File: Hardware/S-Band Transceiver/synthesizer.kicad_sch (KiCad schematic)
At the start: 1 part, among them U10 ADF4351

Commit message: Working on schematic for adf4351
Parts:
- added C10, C11, C12, C20, C23, C25, C27, C29, C31: 10pF, symbol Device:C_Small
- added C13, C14, C15, C21, C22, C24, C26, C28, C30: 100nF, symbol Device:C_Small
- added C16: 39nF, symbol Device:C_Small
- added C17: 2.7nF, symbol Device:C_Small
- added C18: 1.2nF, symbol Device:C_Small
- added C19: 10nF, symbol Device:C_Small
- added J3: SMA, symbol Connector:Conn_Coaxial
- added R5: 4.7k, symbol Device:R_Small_US
- added R6: 680, symbol Device:R_Small_US
- added R7: 360, symbol Device:R_Small_US
- added R8, R9: 0, symbol Device:R_Small_US
- added X1: XO32, Oscillator:Oscillator_SMD_EuroQuartz_XO91-4Pin_7.0x5.0mm, symbol Oscillator:XO32
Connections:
- net SCLK: now reaches U10.1 (CLK)
- net +3V3: now reaches U10.10 (AVDD)
- net +3V3: now also U10.16 (VVCO), U10.17 (VVCO), U10.28 (DVDD), U10.32 (SDVDD), U10.4 (CE), U10.6 (Vp), C20.1, C21.1, C22.1, C23.1, C24.1, C25.1, C26.2, C27.2, C28.2, C29.2, C30.2, C31.2, X1.4 (V+)
- net GND: now reaches U10.11 (AGNDVCO)
- net GND: now also U10.18 (AGNDVCO), U10.21 (AGNDVCO), U10.27 (DGND), U10.31 (SDGND), U10.33 (EP), U10.8 (CPGND), U10.9 (AGND), C10.1, C11.1, C12.1, C13.1, C14.1, C15.1, C20.2, C21.2, C22.2, C23.2, C24.2, C25.2, C26.1, C27.1, C28.1, C29.1, C30.1, C31.1, J3.2 (Ext), R5.2, X1.2 (GND)
- net at U10.19 (TEMP): now also C12.2, C14.2
- net MOSI: now reaches U10.2 (DATA)
- net at U10.20 (VTUNE): now also C18.2, R6.2
- net at U10.22 (RSET): now also R5.1
- net at U10.23 (VCOM): now also C11.2, C13.2
- net at U10.24 (VREF): now also C10.2, C15.2
- net LD: now reaches U10.25 (LD)
- net PDB_RF: now reaches U10.26 (PDB_RF)
- net at U10.29 (REFIN): now also C19.1
- net ~{CS}: now reaches U10.3 (LE)
- net MUXOUT: now reaches U10.30 (MUXOUT)
- net at U10.7 (CPout): now also C16.2, C17.2, R6.1
- new net: C17.1, C18.1, R7.1
- new net: C16.1, R7.2
- new net EXT_REF: J3.1 (In), R9.1
- new net REF_IN: C19.2, R8.2, R9.2
- new net XO_EN: X1.1 (EN)
- new net XO_REF: R8.1, X1.3 (OUT)
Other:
- moved on the sheet: U10

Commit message: Updating schematic
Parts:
- added C44, C50: 100nF, symbol Device:C_Small
- added C45, C46, C49, C51: 120pF, symbol Device:C_Small
- added C47, C48, C52, C53: 1nF, symbol Device:C_Small
- added J5: SMA, symbol Connector:Conn_Coaxial
- added L10, L13, L14, L9: 1.9nH, symbol Device:L_Small
- added L11, L12, L7, L8: 7.5nH, symbol Device:L_Small
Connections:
- net GND: now also C44.2, C45.2, C46.2, C49.2, C50.2, C51.2, J5.2 (Ext)
- net at U10.12 (RF_OUT_A+): now also C52.1, L11.1
- net at U10.13 (RF_OUT_A-): now also C53.1, L12.2
- net at U10.14 (RF_OUT_B+): now also C48.1, L8.1
- net at U10.15 (RF_OUT_B-): now also C47.1, L7.2
- new net: C48.2, L10.1
- new net: C49.1, C50.1, C51.1, L11.2, L12.1
- new net: J5.1 (In), L14.2
- new net: C52.2, L13.1
- new net: C47.2, L9.1
- new net: C53.2, L14.1
- new net: C44.1, C45.1, C46.1, L7.1, L8.2
- new net LO+: L10.2
- new net LO-: L9.2

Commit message: Updating schematic
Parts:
- added C54: 100nF, symbol Device:C_Small
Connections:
- net +3V3: now also C54.1; no longer C24.1, C25.1, C26.2, C27.2, U10.16 (VVCO), U10.17 (VVCO), U10.4 (CE)
- net GND: now also C54.2
- new net +3V3PLL: C24.1, C25.1, C26.2, C27.2, U10.16 (VVCO), U10.17 (VVCO), U10.4 (CE)
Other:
- moved on the sheet: J3, R8, R9, X1

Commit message: Updating schematic
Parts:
- X1: footprint Oscillator:Oscillator_SMD_EuroQuartz_XO91-4Pin_7.0x5.0mm -> Oscillator:Oscillator_SMD_EuroQuartz_XO32-4Pin_3.2x2.5mm
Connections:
- net +3V3PLL: now also C44.1, C45.1, C46.1, C49.1, C50.1, C51.1, L11.2, L12.1, L7.1, L8.2
- net SYNTH_TX: now reaches L13.2
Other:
- note added: "0dBm"
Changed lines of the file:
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@@
 	(wire
 		(pts
+			(xy 214.63 72.39) (xy 215.9 72.39)
+		)
+		(stroke
+			(width 0)
+			(type default)
+		)
+	)
+	(wire
+		(pts
 			(xy 88.9 124.46) (xy 88.9 127)
 		)
@@
 	(wire
 		(pts
+			(xy 245.11 63.5) (xy 248.92 63.5)
+		)
+		(stroke
+			(width 0)
+			(type default)
+		)
+	)
+	(wire
+		(pts
 			(xy 152.4 64.77) (xy 152.4 69.85)
 		)
@@
 	(wire
 		(pts
+			(xy 213.36 121.92) (xy 215.9 121.92)
+		)
+		(stroke
+			(width 0)
+			(type default)
+		)
+	)
+	(wire
+		(pts
 			(xy 60.96 40.64) (xy 63.5 40.64)
 		)
@@
 		)
 	)
+	(text "0dBm"
+		(exclude_from_sim no)
+		(at 255.524 60.706 0)
+		(effects
+			(font
+				(size 1.27 1.27)
+			)
+		)
+	)
 	(global_label "XO_REF"
 		(shape input)
@@
 		)
 	)
+	(global_label "+3V3PLL"
+		(shape input)
+		(at 214.63 72.39 180)
+		(fields_autoplaced yes)
+		(effects
+			(font
+				(size 1.27 1.27)
+			)
+			(justify right)
+		)
+		(property "Intersheetrefs" "${INTERSHEET_REFS}"
+			(at 203.2386 72.39 0)
+			(effects
+				(font
+					(size 1.27 1.27)
+				)
+				(justify right)
+				(hide yes)
+			)
+		)
+	)
+	(global_label "+3V3PLL"
+		(shape input)
+		(at 213.36 121.92 180)
+		(fields_autoplaced yes)
+		(effects
+			(font
+				(size 1.27 1.27)
+			)
+			(justify right)
+		)
+		(property "Intersheetrefs" "${INTERSHEET_REFS}"
+			(at 201.9686 121.92 0)
+			(effects
+				(font
+					(size 1.27 1.27)
+				)
+				(justify right)
+				(hide yes)
+			)
+		)
+	)
 	(global_label "MOSI"
 		(shape input)
@@
 		)
 	)
+	(global_label "SYNTH_TX"
+		(shape input)
+		(at 248.92 63.5 0)
+		(fields_autoplaced yes)
+		(effects
+			(font
+				(size 1.27 1.27)
+			)
+			(justify left)
+		)
+		(property "Intersheetrefs" "${INTERSHEET_REFS}"
+			(at 260.9766 63.5 0)
+			(effects
+				(font
+					(size 1.27 1.27)
+				)
+				(justify left)
+				(hide yes)
+			)
+		)
+	)
 	(global_label "+3V3PLL"
 		(shape input)
@@
 			)
 		)
-		(property "Footprint" "Oscillator:Oscillator_SMD_EuroQuartz_XO91-4Pin_7.0x5.0mm"
+		(property "Footprint" "Oscillator:Oscillator_SMD_EuroQuartz_XO32-4Pin_3.2x2.5mm"
 			(at 57.15 49.53 0)
 			(effects

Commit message: Updating PLL
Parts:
- added D7: LED_Small, symbol Device:LED_Small
- added R49: 1k, symbol Device:R_Small_US
- added R50, R51: 0, symbol Device:R_Small_US
- C16: value 39nF -> 47nF
- C18: value 1.2nF -> 680pF
- R6: value 680 -> 1k
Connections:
- net +3V3PLL: no longer C24.1, C25.1, C26.2, C27.2, U10.16 (VVCO), U10.17 (VVCO), U10.4 (CE)
- net GND: now also C17.1, C18.1, D7.1 (K), R51.1
- net LD: now also R49.1
- net at U10.5 (SW): now also R50.2
- new net: R50.1, R51.2, R7.1
- new net: D7.2 (A), R49.2
- new net +3V3A: C24.1, C25.1, C26.2, C27.2, U10.16 (VVCO), U10.17 (VVCO), U10.4 (CE)
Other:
- note added: "Lock Detect"
- moved on the sheet: C16, C17, C18, R6, R7

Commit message: Updates to schematic
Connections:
- net +3V3PLL is gone; now on net +3.3VA: C44.1, C45.1, C46.1, C49.1, C50.1, C51.1, L11.2, L12.1, L7.1, L8.2
- net +3V3: no longer C54.1, X1.4 (V+)
- net +3V3A renamed +3.3VA
- net +3.3VA: now also C54.1, X1.4 (V+)
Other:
- note added: "RF Power Down"

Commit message: Updates to schematic
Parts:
- added R60: 0, symbol Device:R_Small_US
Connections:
- net +3.3VA: now also R60.2; no longer U10.4 (CE)
- new net SYNTH_CE: R60.1, U10.4 (CE)
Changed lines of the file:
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@@
 	)
 	(junction
+		(at 106.68 96.52)
+		(diameter 0)
+		(color 0 0 0 0)
+	)
+	(junction
 		(at 147.32 54.61)
 		(diameter 0)
@@
 	(wire
 		(pts
-			(xy 110.49 96.52) (xy 124.46 96.52)
+			(xy 106.68 96.52) (xy 124.46 96.52)
 		)
 		(stroke
@@
 	(wire
 		(pts
-			(xy 110.49 96.52) (xy 110.49 91.44)
+			(xy 106.68 92.71) (xy 106.68 96.52)
 		)
 		(stroke
@@
 	(wire
 		(pts
+			(xy 104.14 96.52) (xy 106.68 96.52)
+		)
+		(stroke
+			(width 0)
+			(type default)
+		)
+	)
+	(wire
+		(pts
 			(xy 81.28 119.38) (xy 81.28 116.84)
 		)
@@
 	(wire
 		(pts
+			(xy 106.68 86.36) (xy 106.68 87.63)
+		)
+		(stroke
+			(width 0)
+			(type default)
+		)
+	)
+	(wire
+		(pts
 			(xy 229.87 72.39) (xy 229.87 68.58)
 		)
@@
 		)
 	)
+	(global_label "SYNTH_CE"
+		(shape input)
+		(at 104.14 96.52 180)
+		(fields_autoplaced yes)
+		(effects
+			(font
+				(size 1.27 1.27)
+			)
+			(justify right)
+		)
+		(property "Intersheetrefs" "${INTERSHEET_REFS}"
+			(at 91.8415 96.52 0)
+			(effects
+				(font
+					(size 1.27 1.27)
+				)
+				(justify right)
+				(hide yes)
+			)
+		)
+	)
 	(global_label "REF_IN"
 		(shape input)
@@
 	)
 	(symbol
+		(lib_id "Device:R_Small_US")
+		(at 106.68 90.17 180)
+		(unit 1)
+		(exclude_from_sim no)
+		(in_bom yes)
+		(on_board yes)
+		(dnp no)
+		(property "Reference" "R60"
+			(at 109.728 89.408 0)
+			(effects
+				(font
+					(size 1.27 1.27)
+				)
+			)
+		)
+		(property "Value" "0"
+			(at 109.474 91.948 0)
+			(effects
+				(font
+					(size 1.27 1.27)
+				)
+			)
+		)
+		(property "Footprint" ""
+			(at 106.68 90.17 0)
+			(effects
+				(font
+					(size 1.27 1.27)
+				)
+				(hide yes)
+			)
+		)
+		(property "Datasheet" "~"
+			(at 106.68 90.17 0)
+			(effects
+				(font
+					(size 1.27 1.27)
+				)
+				(hide yes)
+			)
+		)
+		(property "Description" "Resistor, small US symbol"
+			(at 106.68 90.17 0)
+			(effects
+				(font
+					(size 1.27 1.27)
+				)
+				(hide yes)
+			)
+		)
+		(pin "2"
+		)
+		(pin "1"
+		)
+		(instances
+			(project "S-Band Transceiver"
+				(path "/811f57cf-e3df-4fba-aff9-353adc85299e/1f8ad4e6-608c-455a-8c5c-ffe69657f316"
+					(reference "R60")
+					(unit 1)
+				)
+			)
+		)
+	)
+	(symbol
 		(lib_id "power:GND")
 		(at 92.71 128.27 0)
@@
 	(symbol
 		(lib_id "power:+3.3VA")
-		(at 110.49 91.44 0)
+		(at 106.68 86.36 0)
 		(unit 1)
 		(exclude_from_sim no)
@@
 		(dnp no)
 		(property "Reference" "#PWR0127"
-			(at 110.49 95.25 0)
+			(at 106.68 90.17 0)
 			(effects
 				(font
@@
 		)
 		(property "Value" "+3.3VA"
-			(at 110.49 87.122 0)
+			(at 106.68 82.042 0)
 			(effects
 				(font
@@
 		)
 		(property "Footprint" ""
-			(at 110.49 91.44 0)
+			(at 106.68 86.36 0)
 			(effects
 				(font
@@
 		)
 		(property "Datasheet" ""
-			(at 110.49 91.44 0)
+			(at 106.68 86.36 0)
 			(effects
 				(font
@@
 		)
 		(property "Description" "Power symbol creates a global label with name \"+3.3VA\""
-			(at 110.49 91.44 0)
+			(at 106.68 86.36 0)
 			(effects
 				(font

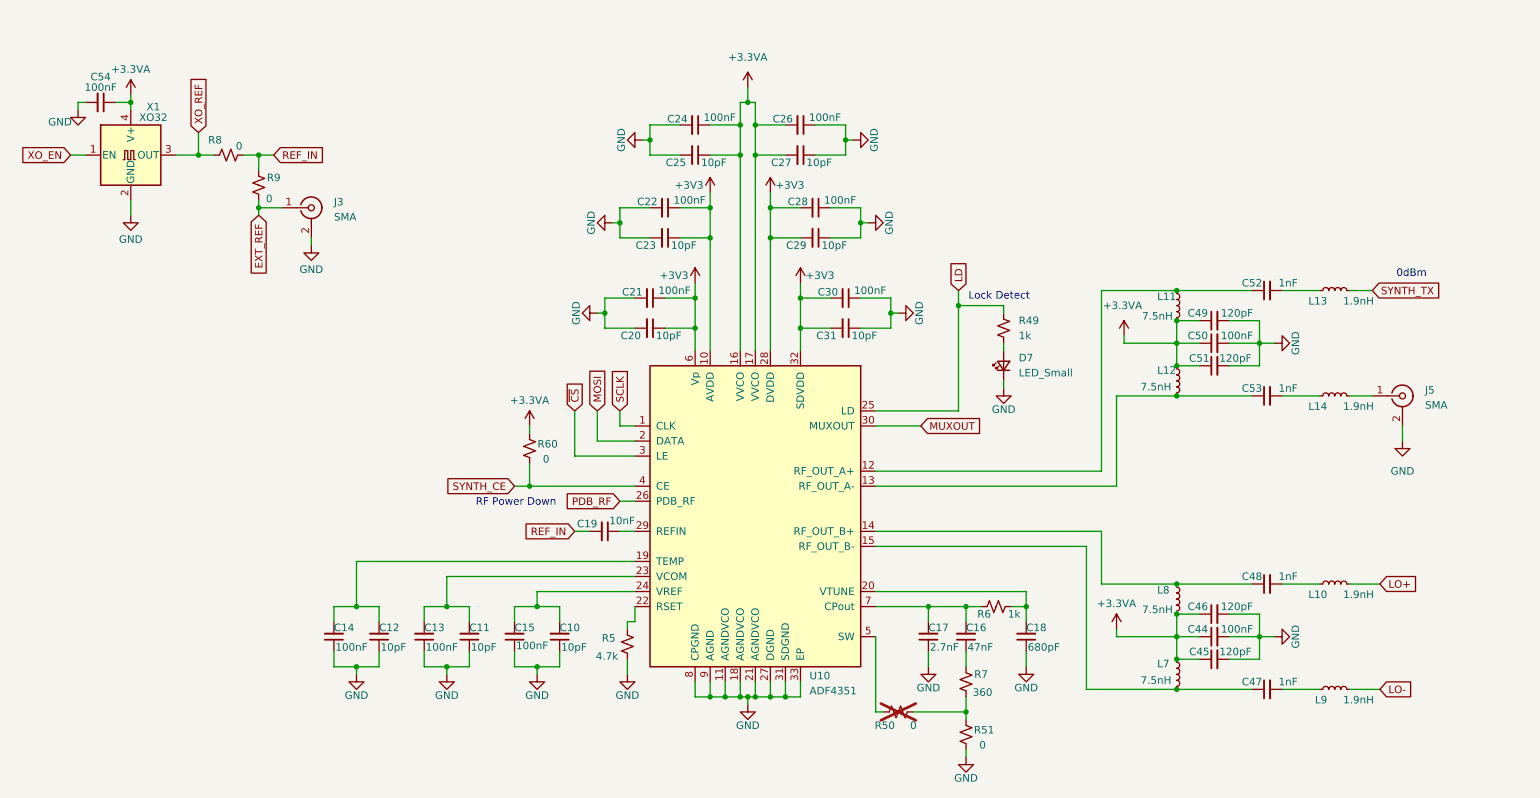
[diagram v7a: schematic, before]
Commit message: Updates to Schematic
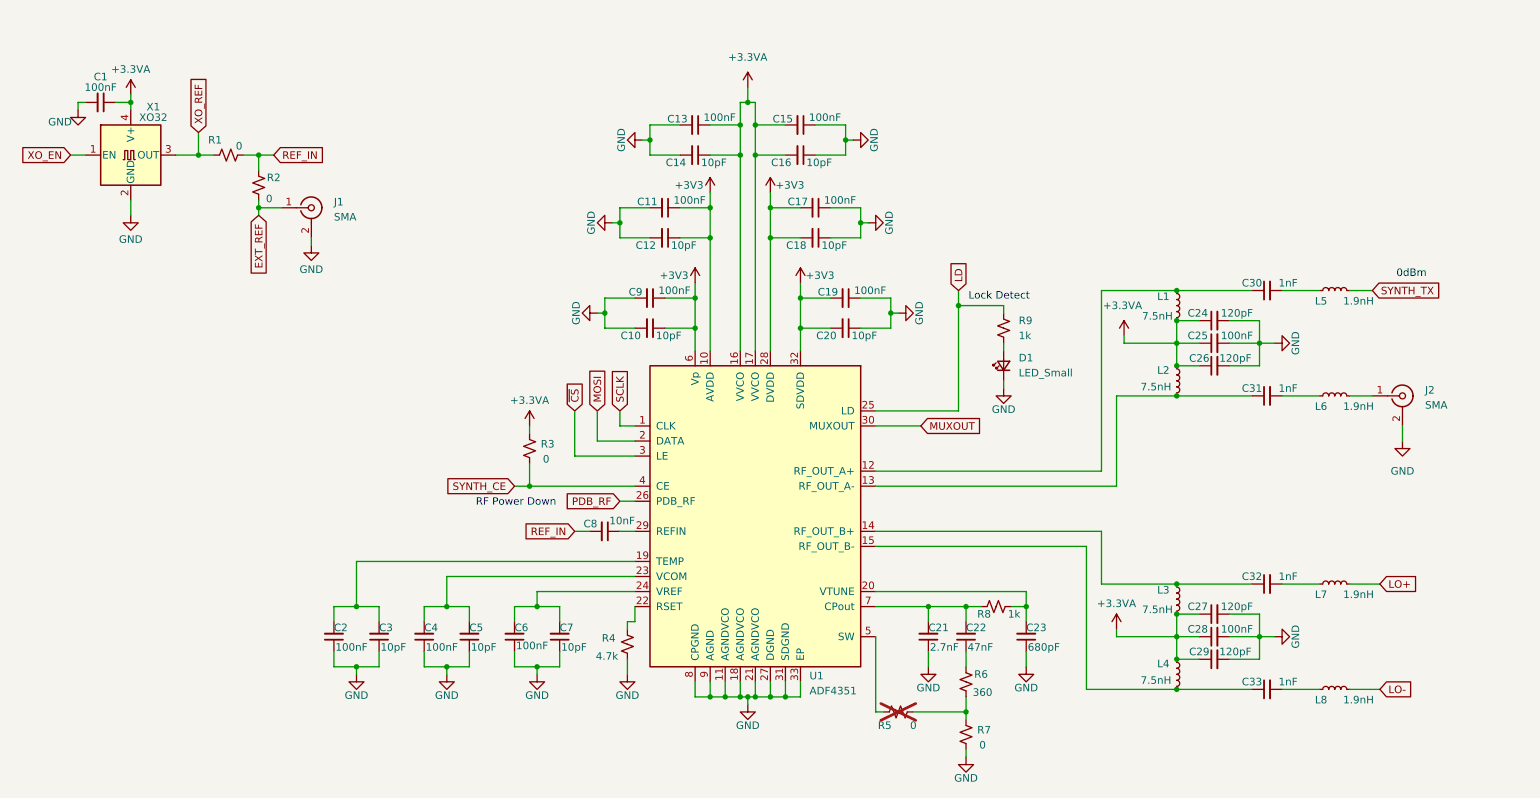
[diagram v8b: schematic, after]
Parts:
- renumbered C54 to C1, C20 to C10, C22 to C11, C23 to C12, C24 to C13, C25 to C14, C26 to C15, C27 to C16, C28 to C17, C29 to C18, C30 to C19, C14 to C2, C31 to C20, C17 to C21, C16 to C22, C18 to C23, C49 to C24, C50 to C25, C51 to C26, C46 to C27, C44 to C28, C45 to C29, C12 to C3, C52 to C30, C53 to C31, C48 to C32, C47 to C33, C13 to C4, C11 to C5, C15 to C6, C10 to C7, C19 to C8, C21 to C9, D7 to D1, J3 to J1, J5 to J2, L11 to L1, L12 to L2, L8 to L3, L7 to L4, L13 to L5, L14 to L6, L10 to L7, L9 to L8, R8 to R1, R9 to R2, R60 to R3, R5 to R4, R50 to R5, R7 to R6, R51 to R7, R6 to R8, R49 to R9, U10 to U1
